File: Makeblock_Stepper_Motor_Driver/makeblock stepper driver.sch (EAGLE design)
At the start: 7 parts, among them IC1 A4988SETTR-T

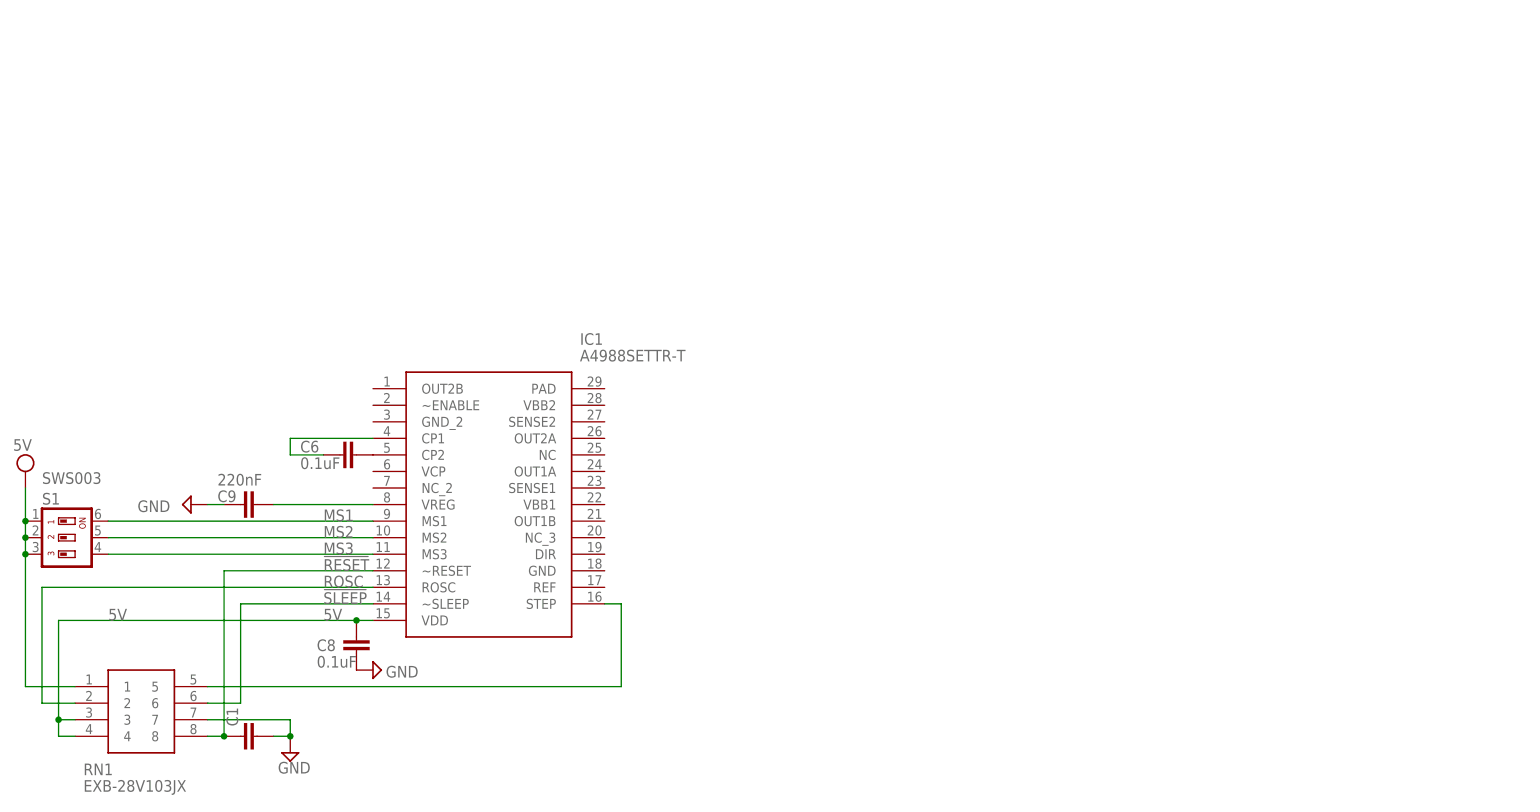
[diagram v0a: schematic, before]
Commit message: Added parts to the schematic
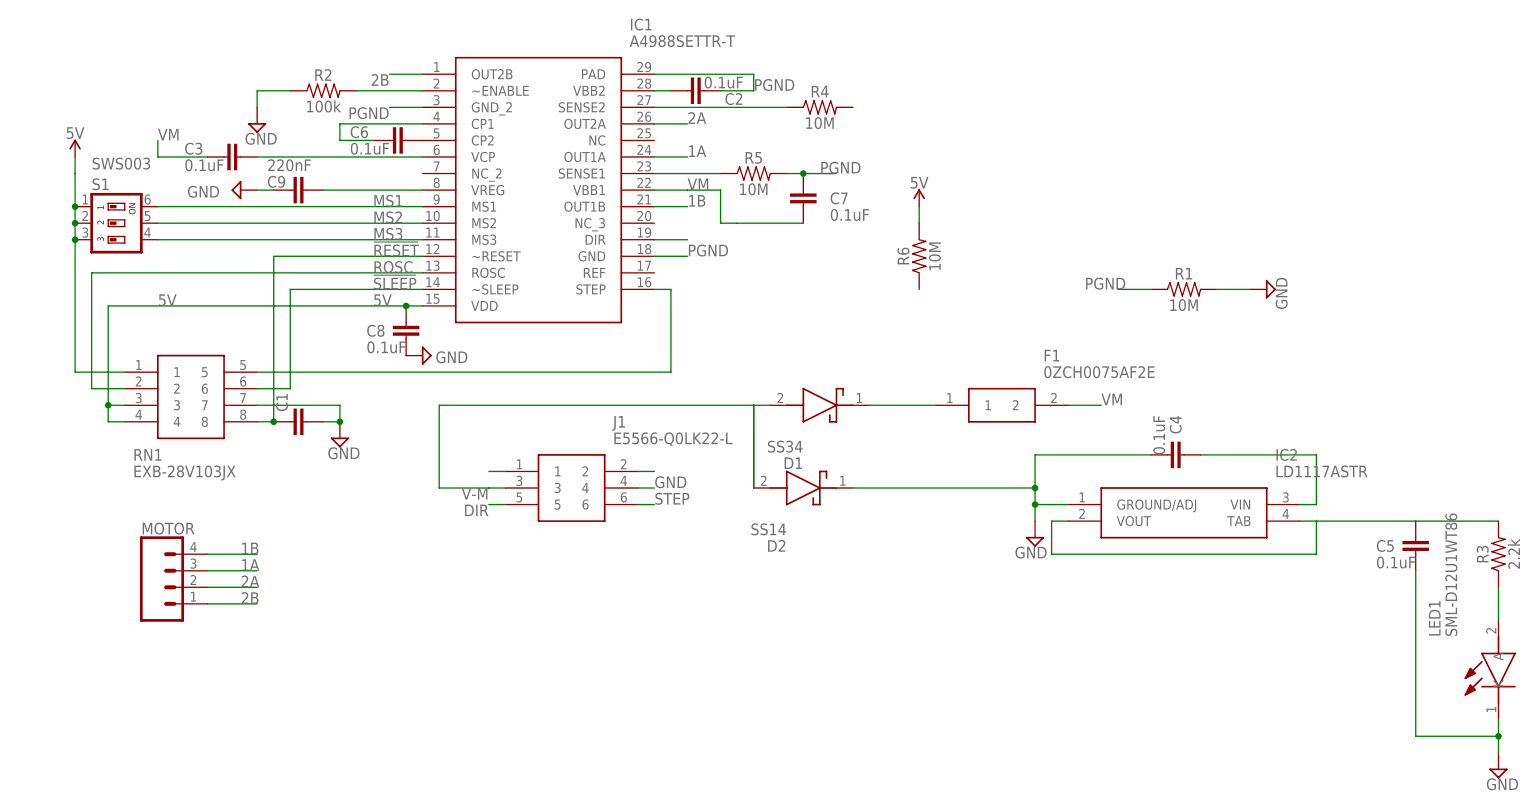
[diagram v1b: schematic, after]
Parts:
- added C2, C3, C4, C5, C7: 0.1uF, resistor:C-EUC0402
- added D1: SS34, SamacSys_Parts:SS34
- added D2: SS14, SamacSys_Parts:SS14
- added F1: 0ZCH0075AF2E, SamacSys_Parts:0ZCH0075AF2E
- added IC2: LD1117ASTR, SamacSys_Parts:LD1117ASTR
- added J1: E5566-Q0LK22-L, SamacSys_Parts:E5566-Q0LK22-L
- added LED1: SML-D12U1WT86, SamacSys_Parts:SML-D12U1WT86
- added MOTOR: (no value), SparkFun-Connectors:CONN_04JST-PTH-VERT
- added R1, R4, R5, R6: 10M, SparkFun-Resistors:10MOHM-0603-1/10W-5%
- added R2: 100k, SparkFun-Resistors:10MOHM-0603-1/10W-5%
- added R3: 2.2k, SparkFun-Resistors:10MOHM-0603-1/10W-5%
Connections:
- removed net VCC: RN1.1, S1.1, S1.2, S1.3
- new net 1A: IC1.OUT1A, MOTOR.3
- new net 1B: IC1.OUT1B, MOTOR.4
- new net 2A: IC1.OUT2A, MOTOR.2
- new net 2B: IC1.OUT2B, MOTOR.1
- new net DIR: J1.5
- new net N$10: LED1.A, R3.1
- new net N$11: C5.2, IC2.TAB, IC2.VOUT, R3.2
- new net N$12: IC1.~ENABLE, R2.2
- new net N$13: C3.2, IC1.VCP
- new net N$14: IC1.SENSE2, R4.1
- new net N$15: IC1.SENSE1, R5.1
- new net N$16: IC1.DIR
- new net N$3: J1.1
- new net N$4: C2.2, IC1.VBB2
- new net N$5: D1.K, F1.1
- new net N$6: C4.2, IC2.VIN
- new net N$9: J1.2
- new net PGND: C2.1, C7.1, IC1.GND, IC1.GND_2, IC1.PAD, R1.1, R5.2
- new net STEP: J1.6
- new net V-M: D1.A, D2.A, J1.3
- new net VM: C3.1, C7.2, F1.2, IC1.VBB1
- net 5V: now also R6.2, RN1.1, S1.1, S1.2, S1.3
- net GND: now also C4.1, C5.1, D2.K, IC2.GROUND/ADJ, J1.4, LED1.K, R1.2, R2.1
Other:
- moved on the sheet: C1, C6, C8, C9, IC1, RN1, S1

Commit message: Finshed the schematic and the layout
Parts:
- added C10: 0.1u, resistor:C-EUC0402
- added P2: (no value), SparkFun-Connectors:CONN_04PTH
- added P3: (no value), SparkFun-Connectors:CONN_03LOCK
- added R7: 0.2R, SparkFun-Resistors:10MOHM-0603-1/10W-5%
- C1: value (none) -> 0.1uF
- C3: value 0.1uF -> 22uF; device resistor:C-EUC0402 -> rcl:C-US025-024X044
- R1: value 10M -> 0.2R
- R2: value 100k -> 0.2R
- R4: value 10M -> 27k
- R5: value 10M -> 100k
- R6: value 10M -> PVG3A203C01R00; device SparkFun-Resistors:10MOHM-0603-1/10W-5% -> SamacSys_Parts:PVG3A203C01R00
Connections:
- removed net N$12: IC1.~ENABLE, R2.2
- removed net N$4: C2.2, IC1.VBB2
- removed net ROSC: IC1.ROSC, RN1.2
- new net EN: IC1.~ENABLE, P3.1, R5.2
- new net N$17: IC1.REF, R6.2
- net !RESET: now also C10.1, P3.2; no longer C1.1
- net !SLEEP: now also P3.3
- net 5V: now also R4.2; no longer R6.2
- net DIR: now also IC1.DIR, P2.2
- net GND: now also C10.2, P2.3, R5.1, R6.3, R7.2, RN1.2; no longer C1.2, C9.1, D2.K, R1.2, R2.1, RN1.7
- net N$13: now also C7.2; no longer C3.2
- net N$14: now also R1.1; no longer R4.1
- net N$15: now also R2.1; no longer R5.1
- net N$16: now also R4.1, R6.1; no longer IC1.DIR
- net N$6: now also D2.K
- net N$8: now also IC1.ROSC, RN1.7; no longer IC1.STEP, RN1.5
- net PGND: now also C1.1, C3.2, C9.1, R2.2, R7.1; no longer C7.1, R1.1, R5.2
- net STEP: now also IC1.STEP, P2.1, RN1.5
- net V-M: now also P2.4
- net VM: now also C1.2, C2.2, C7.1, IC1.VBB2; no longer C7.2
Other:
- moved on the sheet: C1, C2, C3, C4, C7, D2, R1, R2, R4, R5
